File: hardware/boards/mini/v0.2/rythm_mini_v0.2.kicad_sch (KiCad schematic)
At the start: 90 parts, among them IC1 NAU88C22YG, IC3 IS42S16160J-6BLI, J1 Bottom, J3 Top, Q1 PMV37EN22, U1 W25Q128JVP, U2 LTV-217-G, U4 STM32H750XBHx, Y1 Crystal_GND24

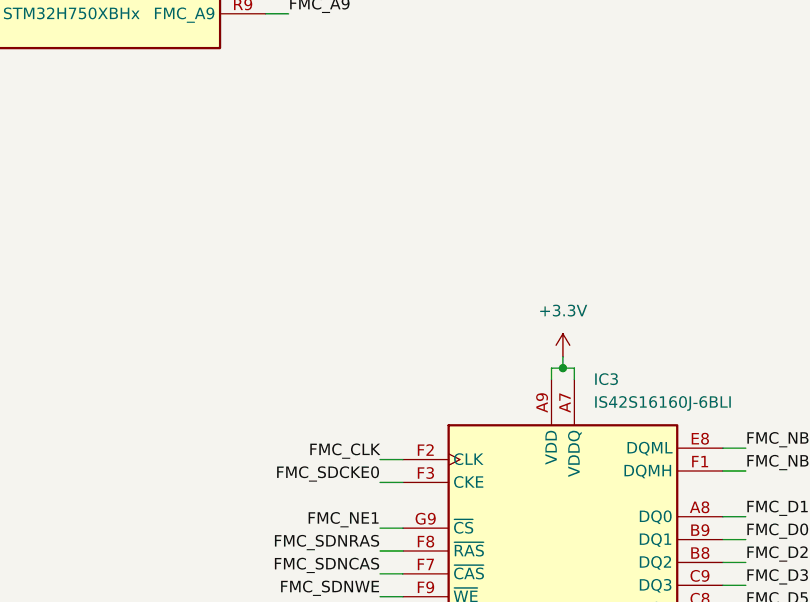
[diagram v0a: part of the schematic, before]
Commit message: mini: add SDRAM decoupling
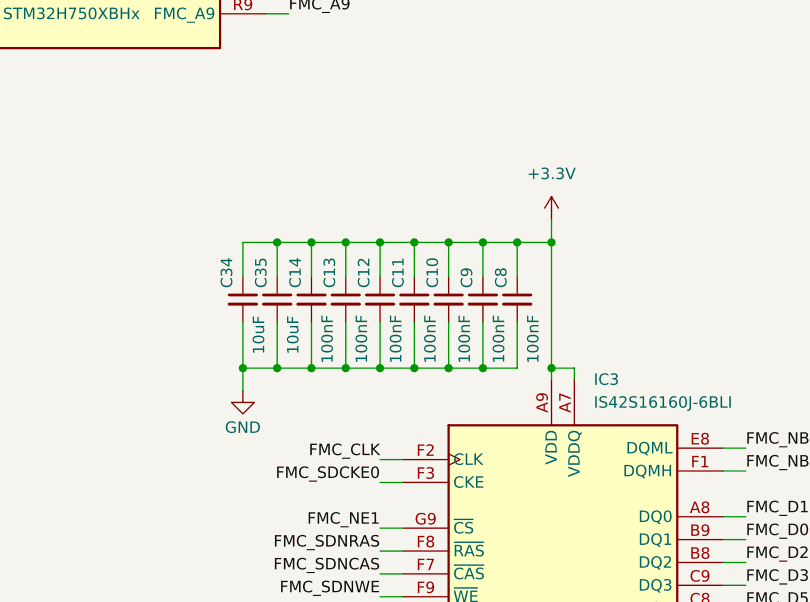
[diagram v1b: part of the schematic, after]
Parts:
- added C10, C11, C12, C13, C14, C8, C9: 100nF, Capacitor_SMD:C_0402_1005Metric, symbol Device:C_Small
- added C34, C35: 10uF, Capacitor_SMD:C_0402_1005Metric, symbol Device:C_Small
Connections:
- net +3.3V: now also C10.1, C11.1, C12.1, C13.1, C14.1, C34.1, C35.1, C8.1, C9.1
- net GND: now also C10.2, C11.2, C12.2, C13.2, C14.2, C34.2, C35.2, C8.2, C9.2

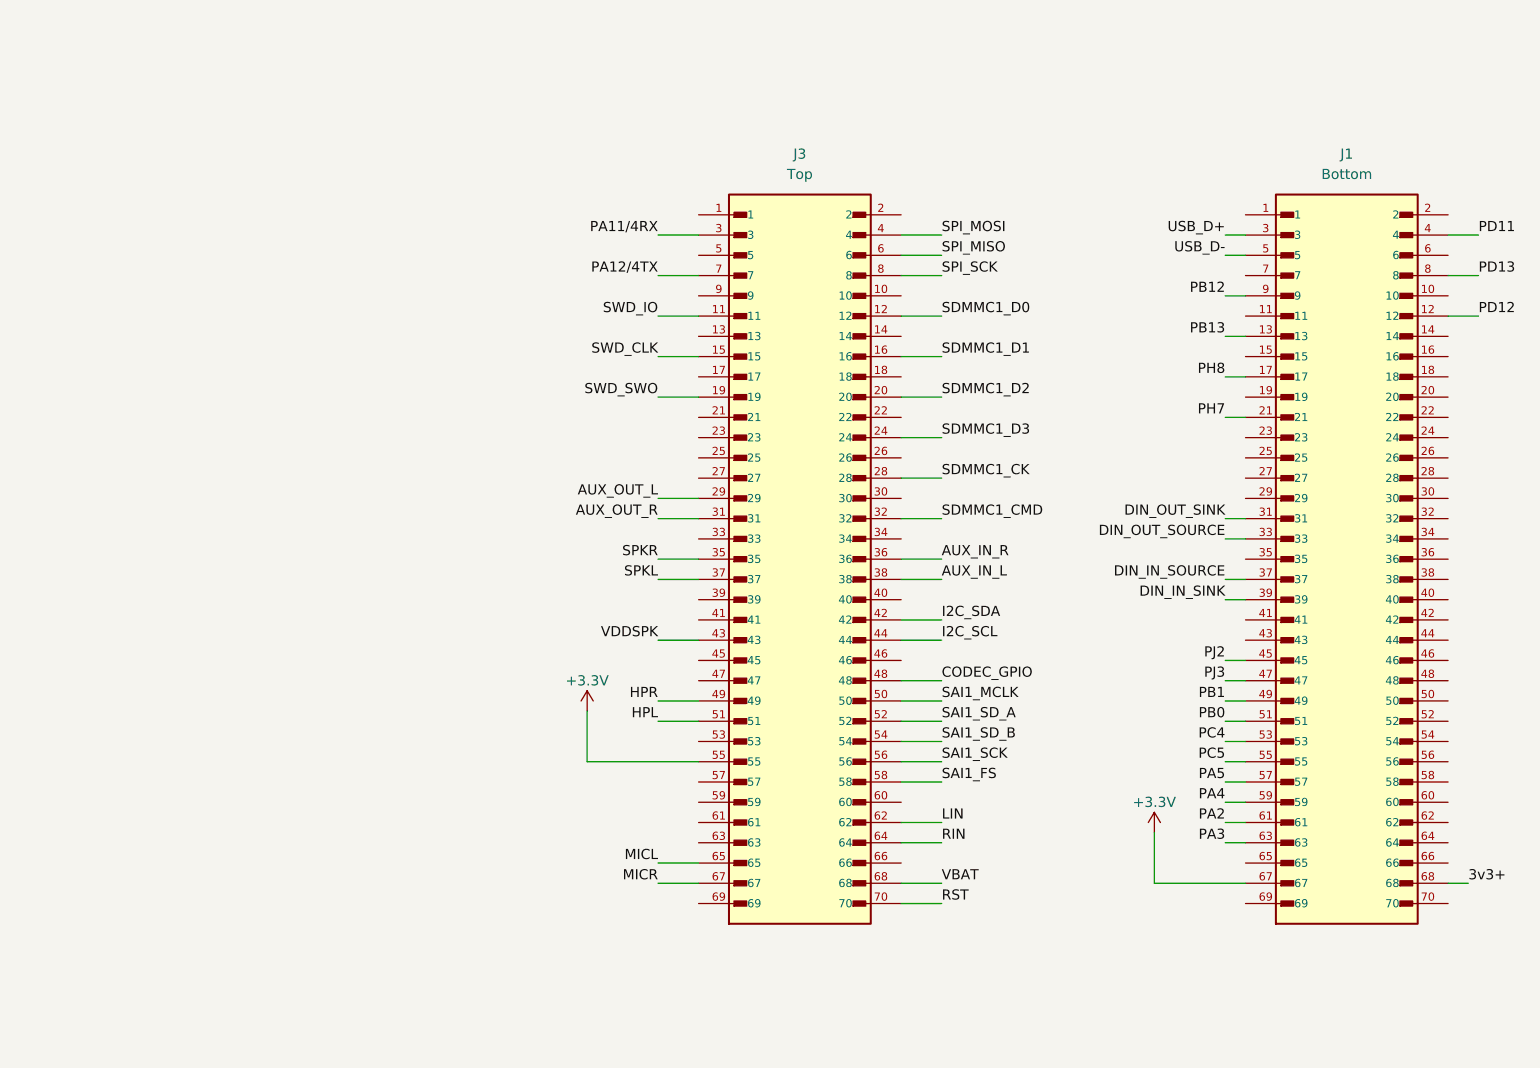
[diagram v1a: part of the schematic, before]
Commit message: mini: downsized mezzanine from 70 pin to 60
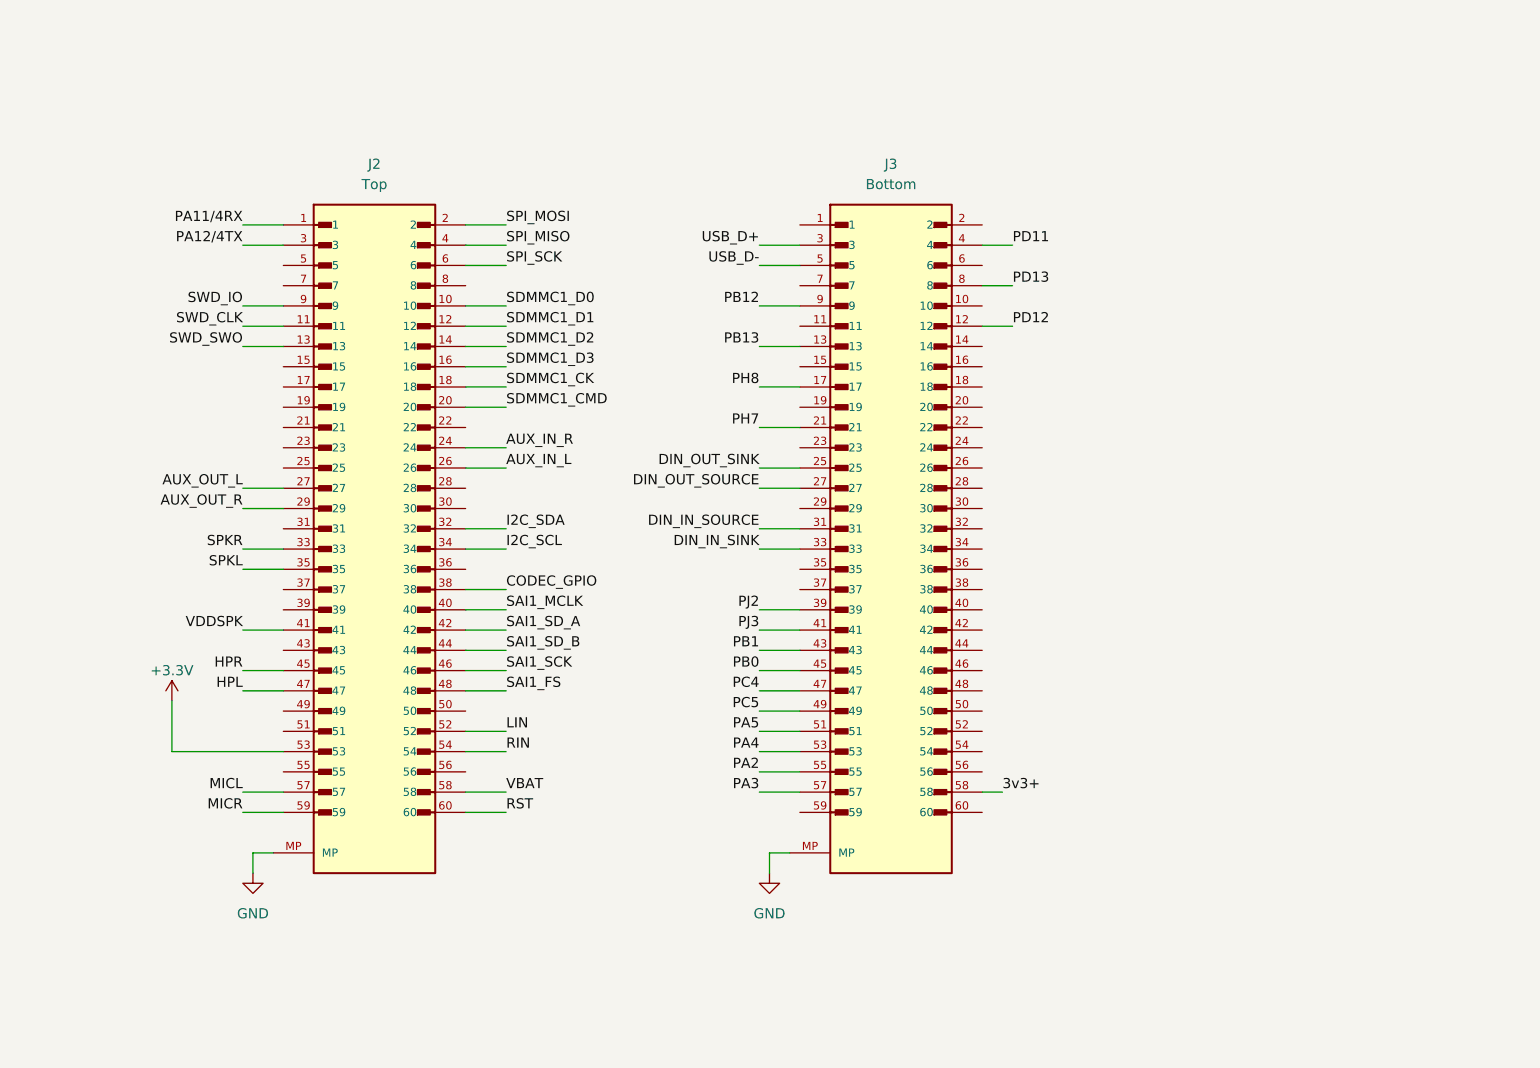
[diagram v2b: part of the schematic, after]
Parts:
- removed J1: Bottom, Connector_Hirose_DF40:Hirose_DF40C-70DP-0.4V_2x35-1MP_P0.4mm, symbol DF40C-70DP-0.4V_51_:DF40C-70DP-0.4V_51_
- removed J3: Top, Connector_Hirose_DF40:Hirose_DF40C-70DP-0.4V_2x35-1MP_P0.4mm, symbol DF40C-70DP-0.4V_51_:DF40C-70DP-0.4V_51_
- added J2: Top, Connector_Hirose_DF40:Hirose_DF40C-60DP-0.4V_2x30-1MP_P0.4mm, symbol DF40C-60DP-0.4V_51_:DF40C-60DP-0.4V_51_
- added J3: Bottom, Connector_Hirose_DF40:Hirose_DF40C-60DP-0.4V_2x30-1MP_P0.4mm, symbol DF40C-60DP-0.4V_51_:DF40C-60DP-0.4V_51_
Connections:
- net +3.3V: now also J2.53
- net 3v3+: now also J3.58
- net AUX_IN_L: now also J2.26
- net AUX_IN_R: now also J2.24
- net AUX_OUT_L: now also J2.27
- net AUX_OUT_R: now also J2.29
- net CODEC_GPIO: now also J2.38
- net DIN_IN_SINK: now also J3.33
- net DIN_IN_SOURCE: now also J3.31
- net DIN_OUT_SINK: now also J3.25
- net DIN_OUT_SOURCE: now also J3.27
- net GND: now also J2.MP, J3.MP
- net HPL: now also J2.47
- net HPR: now also J2.45
- net I2C_SCL: now also J2.34
- net I2C_SDA: now also J2.32
- net LIN: now also J2.52
- net MICL: now also J2.57
- net MICR: now also J2.59
- net PA11/4RX: now also J2.1
- net PA12/4TX: now also J2.3
- net PA2: now also J3.55
- net PA3: now also J3.57
- net PA4: now also J3.53
- net PA5: now also J3.51
- net PB0: now also J3.45
- net PB1: now also J3.43
- net PB12: now also J3.9
- net PB13: now also J3.13
- net PC4: now also J3.47
- net PC5: now also J3.49
- net PD11: now also J3.4
- net PD12: now also J3.12
- net PD13: now also J3.8
- net PH7: now also J3.21
- net PH8: now also J3.17
- net PJ2: now also J3.39
- net PJ3: now also J3.41
- net RIN: now also J2.54
- net RST: now also J2.60
- net SAI1_FS: now also J2.48
- net SAI1_MCLK: now also J2.40
- net SAI1_SCK: now also J2.46
- net SAI1_SD_A: now also J2.42
- net SAI1_SD_B: now also J2.44
- net SDMMC1_CK: now also J2.18
- net SDMMC1_CMD: now also J2.20
- net SDMMC1_D0: now also J2.10
- net SDMMC1_D1: now also J2.12
- net SDMMC1_D2: now also J2.14
- net SDMMC1_D3: now also J2.16
- net SPI_MISO: now also J2.4
- net SPI_MOSI: now also J2.2
- net SPI_SCK: now also J2.6
- net SPKL: now also J2.35
- net SPKR: now also J2.33
- net SWD_CLK: now also J2.11
- net SWD_IO: now also J2.9
- net SWD_SWO: now also J2.13
- net USB_D+: now also J3.3
- net USB_D-: now also J3.5
- net VBAT: now also J2.58
- net VDDSPK: now also J2.41
